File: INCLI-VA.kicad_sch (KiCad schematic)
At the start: 5 parts

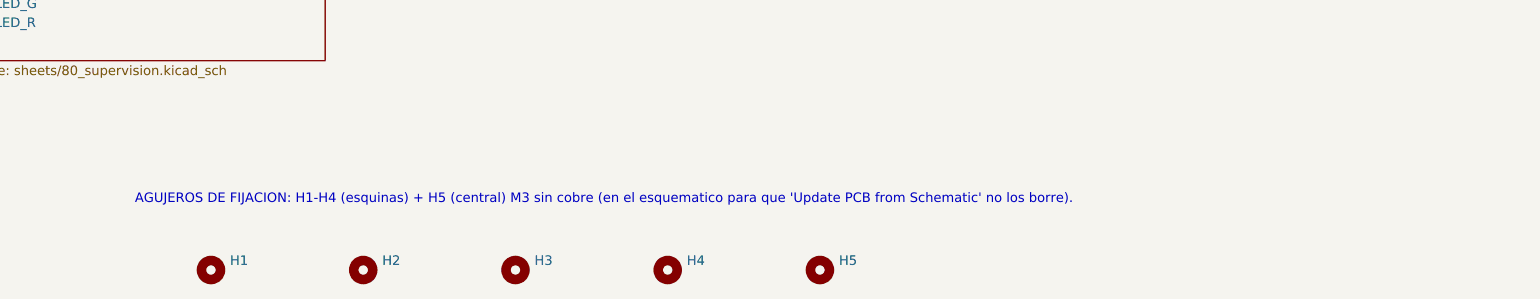
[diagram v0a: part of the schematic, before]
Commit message: [Codex] Retira H5 del esquematico y cierra revision para layout 100x100
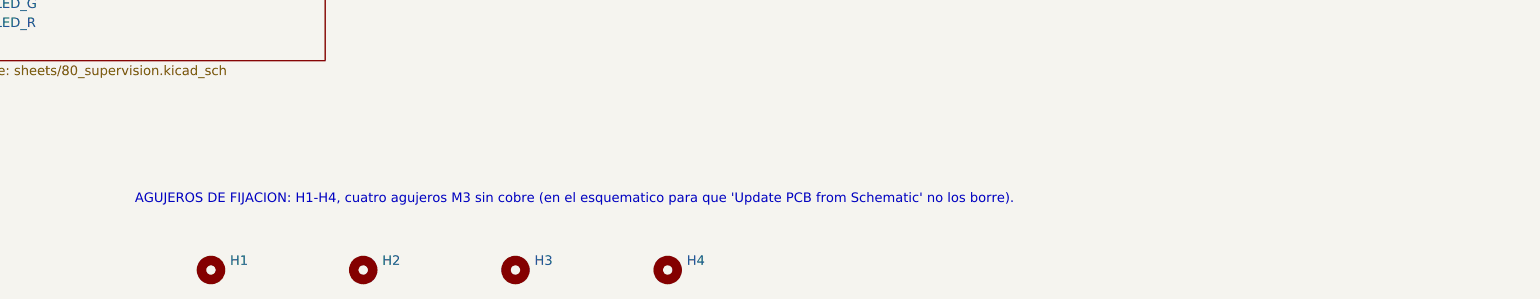
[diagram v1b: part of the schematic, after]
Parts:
- removed H5: MountingHole_M3, MountingHole:MountingHole_3.2mm_M3, symbol Mechanical:MountingHole
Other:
- note added: "AGUJEROS DE FIJACION: H1-H4, cuatro agujeros M3 sin cobre (en el esquematico para que 'Update PCB from Schematic' no los borre)."
- note removed: "AGUJEROS DE FIJACION: H1-H4 (esquinas) + H5 (central) M3 sin cobre (en el esquematico para que 'Update PCB from Schematic' no los borre)."
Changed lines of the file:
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@@
 		)
 	)
-	(text "AGUJEROS DE FIJACION: H1-H4 (esquinas) + H5 (central) M3 sin cobre (en el esquematico para que 'Update PCB from Schematic' no los borre)."
+	(text "AGUJEROS DE FIJACION: H1-H4, cuatro agujeros M3 sin cobre (en el esquematico para que 'Update PCB from Schematic' no los borre)."
 		(exclude_from_sim no)
 		(at 50.8 246.38 0)
@@
 		)
 	)
-	(symbol
-		(lib_id "Mechanical:MountingHole")
-		(at 142.24 256.54 0)
-		(unit 1)
-		(body_style 1)
-		(exclude_from_sim no)
-		(in_bom no)
-		(on_board yes)
-		(in_pos_files yes)
-		(dnp no)
-		(property "Reference" "H5"
-			(at 144.78 255.27 0)
-			(show_name no)
-			(do_not_autoplace no)
-			(effects
-				(font
-					(size 1.27 1.27)
-				)
-				(justify left)
-			)
-		)
-		(property "Value" "MountingHole_M3"
-			(at 144.78 257.81 0)
-			(show_name no)
-			(do_not_autoplace no)
-			(effects
-				(hide yes)
-				(font
-					(size 1.27 1.27)
-				)
-				(justify left)
-			)
-		)
-		(property "Footprint" "MountingHole:MountingHole_3.2mm_M3"
-			(at 142.24 256.54 0)
-			(hide yes)
-			(show_name no)
-			(do_not_autoplace no)
-			(effects
-				(font
-					(size 1.27 1.27)
-				)
-			)
-		)
-		(property "Datasheet" "https://www.kicad.org/libraries/"
-			(at 142.24 256.54 0)
-			(hide yes)
-			(show_name no)
-			(do_not_autoplace no)
-			(effects
-				(font
-					(size 1.27 1.27)
-				)
-			)
-		)
-		(property "Description" ""
-			(at 142.24 256.54 0)
-			(hide yes)
-			(show_name no)
-			(do_not_autoplace no)
-			(effects
-				(font
-					(size 1.27 1.27)
-				)
-			)
-		)
-		(property "MPN" "N/A (agujero NPTH)"
-			(at 142.24 256.54 0)
-			(hide yes)
-			(show_name no)
-			(do_not_autoplace no)
-			(effects
-				(font
-					(size 1.27 1.27)
-				)
-			)
-		)
-		(property "Manufacturer" "N/A"
-			(at 142.24 256.54 0)
-			(hide yes)
-			(show_name no)
-			(do_not_autoplace no)
-			(effects
-				(font
-					(size 1.27 1.27)
-				)
-			)
-		)
-		(property "DNP" ""
-			(at 142.24 256.54 0)
-			(hide yes)
-			(show_name no)
-			(do_not_autoplace no)
-			(effects
-				(font
-					(size 1.27 1.27)
-				)
-			)
-		)
-		(property "Notes" "Agujero CENTRAL de fijacion M3 (3.2 mm), SIN cobre: sube la primera resonancia de la placa (con solo 4 esquinas, estimada en 150-200 Hz, dentro de la banda de ISO 16750-3). Ubicarlo cerca de U501 (inclinometro). Posicion: la define el layout."
-			(at 142.24 256.54 0)
-			(hide yes)
-			(show_name no)
-			(do_not_autoplace no)
-			(effects
-				(font
-					(size 1.27 1.27)
-				)
-			)
-		)
-		(instances
-			(project "INCLI-VA"
-				(path "/7fd92c2b-4254-4d73-93ba-bfde861bede3"
-					(reference "H5")
-					(unit 1)
-				)
-			)
-		)
-	)
